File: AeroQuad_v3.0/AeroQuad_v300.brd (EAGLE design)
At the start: 87.3 x 54.6 mm, 68 parts, among them U1 MPU-6050-1

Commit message: Eagle files including CAM file for latest beta run of AeroQuad32 boards.
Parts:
- removed ACCEL: BMA180, SparkFun:1X08_LOCK
- removed GYRO: ITG3200, SparkFun:1X07_LOCK
- removed LED: ULN2003A, CaranchoEngineering:DIL16
- removed LED_GND, LED_PWR: (no value), SparkFun:1X07_LOCK
- moved LEVELSHIFTIN 72.4 mm to (64.8, 41.9)
- moved LEVELSHIFTOUT 72.4 mm to (64.8, 31.8)
- moved SJ3 11.4 mm to (73.7, 24.1)
- moved R2 9.25 mm to (68.6, 19.1)
- moved SJ2 8.03 mm to (76.2, 24.1)
- moved R1 5.68 mm to (68.6, 20.3)
- moved U1 5.24 mm to (63.5, 25.4)
- moved C2 2.54 mm to (59.7, 17.8)
- moved SJ1 1.80 mm to (74.9, 26.7)
- moved C1 1.27 mm to (59.7, 21.6)
- moved C3 1.27 mm to (59.7, 19.1)
- moved C4 1.27 mm to (59.7, 20.3)
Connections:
- removed net N$10: LED.10, LED_GND.7
- removed net N$11: LED.11, LED_GND.6
- removed net N$12: LED.12, LED_GND.5
- removed net N$13: LED.13, LED_GND.4
- removed net N$14: LED.14, LED_GND.3
- removed net N$17: LED.15, LED_GND.2
- removed net P$16: LED.16, LED_GND.1
- net 3.3V: no longer ACCEL.1, ACCEL.4, ACCEL.8, GYRO.6, GYRO.7
- net GND: no longer ACCEL.2, ACCEL.6, GYRO.3, GYRO.5, LED.8
- net LED1: no longer LED.7
- net LED2: no longer LED.6
- net LED3: no longer LED.5
- net LED4: no longer LED.4
- net LED5: no longer LED.3
- net LED6: no longer LED.2
- net LED7: no longer LED.1
- net SCL-L: no longer ACCEL.5, GYRO.1
- net SDA-L: no longer ACCEL.7, GYRO.2
- net VIN: no longer LED_PWR.1, LED_PWR.2, LED_PWR.3, LED_PWR.4, LED_PWR.5, LED_PWR.6, LED_PWR.7
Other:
- board text added: "MOTOR OUTPUT"
- board text added: "RECEIVER INPUT"
- board text removed: "12V LED"
- board text removed: "ACCELEROMETER"
- board text removed: "GYRO"
- board text removed: "PWM ESC"
- board text removed: "RECEIVER"

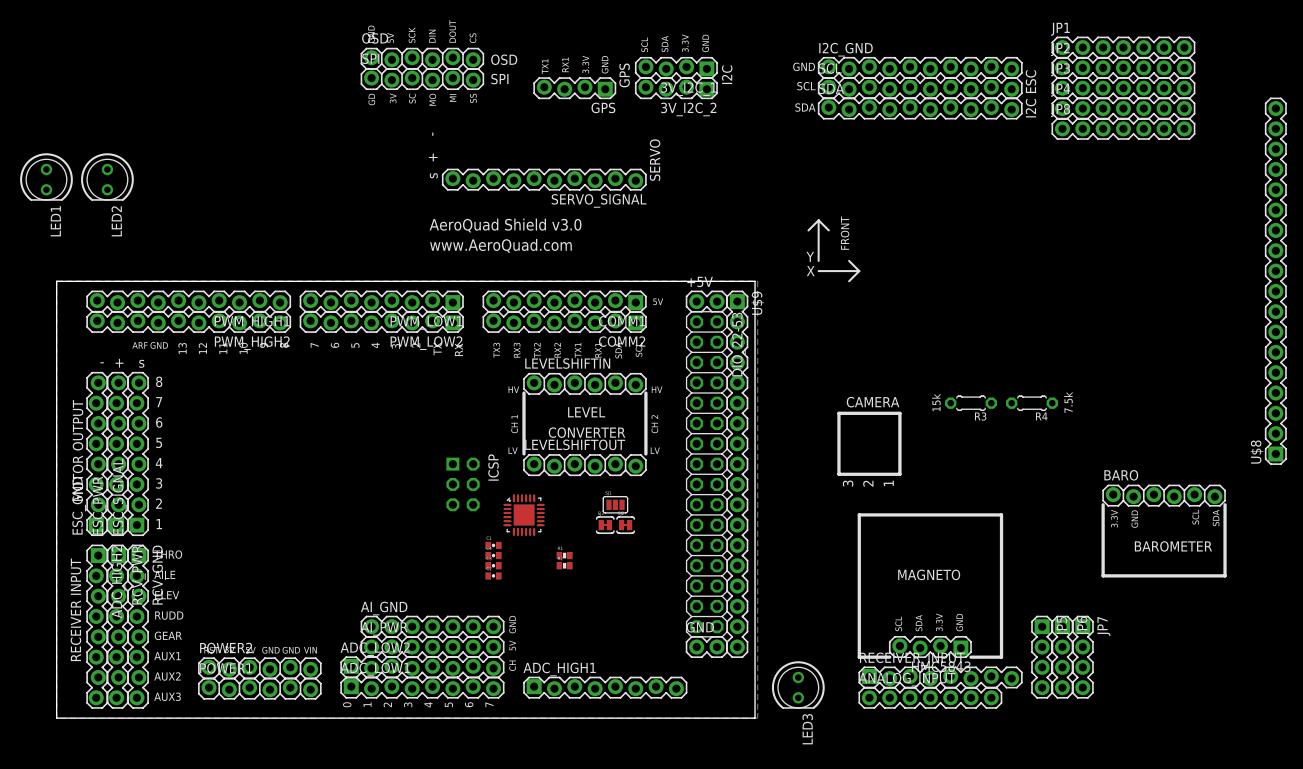
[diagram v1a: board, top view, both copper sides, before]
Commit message: reviewed MPU6000 circuit and connections to Due
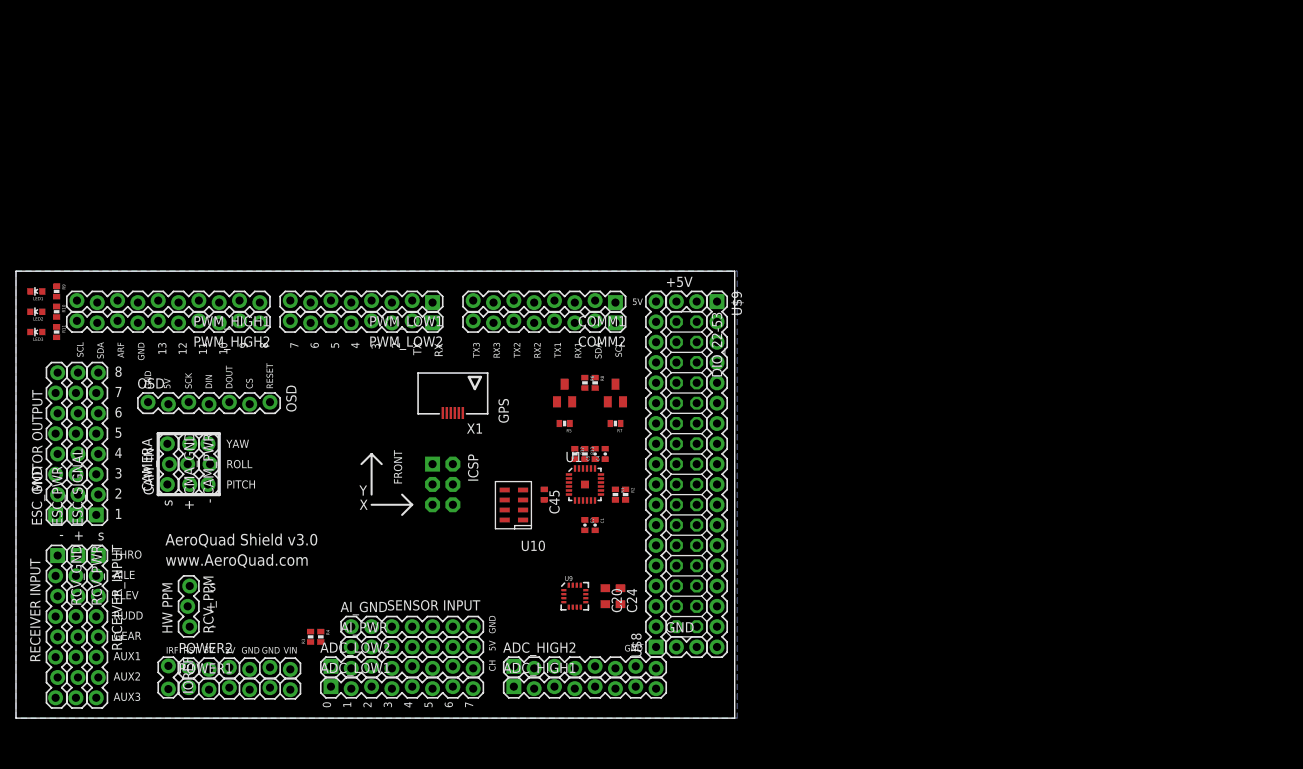
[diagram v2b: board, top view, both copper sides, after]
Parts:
- removed 3V_I2C_1, 3V_I2C_2, GPS, HMC5843: (no value), SparkFun:1X04_LOCK
- removed ANALOG_INPUT, JP1, JP2, JP3, JP4, JP8: (no value), SparkFun:1X07
- removed BARO: BMP085, SparkFun:1X06_LOCK
- removed C3: 0.1uF, SparkFun:0402-CAP
- removed I2C_GND, SCL, SDA, SERVO_SIGNAL: M10LOCK, SparkFun:1X10_LOCK
- removed JP5, JP6, JP7: (no value), SparkFun:1X04
- removed LEVELSHIFTIN, LEVELSHIFTOUT, SPI: (no value), SparkFun:1X06_LOCK
- removed SJ1: (no value), SparkFun:SJ_3_PASTE2&3
- removed SJ2, SJ3: (no value), SparkFun:SJ_2S-TRACE
- added C20, C24: 1uF (ESR), rcl:SMC_Z
- added C45: 0.1uF, rcl:C0402
- added C5: 2.2nF, SparkFun:0402-CAP
- added CAM_IN, CAM_PWR, CMA_GND, RCV_PPM: (no value), SparkFun:1X03_LOCK
- added IOREF: (no value), SparkFun:1X02_LOCK
- added R10, R11, R9: 1k, SparkFun:0402-RES
- added R12, R13, R5, R6, R7, R8: 10k, SparkFun:0402-RES
- added U$1, U$2: BSS138, ava:BSS138
- added U10: MS5611, DSP-TI:LGA08A
- added U9: HMC5883LSMD, SparkFun:16LPCC
- added X1: 06FLZ-SM1, con-jst:6FLZ-SM
- C1: value 0.1uF -> 10nF
- C2: value 2.2nF -> 0.1uF
- C4: value 10nF -> 0.1uF
- LED1: value (none) -> Green; device SparkFun:LED5MM -> SparkFun:LED-0603
- LED2: value (none) -> Yellow; device SparkFun:LED5MM -> SparkFun:LED-0603
- LED3: value (none) -> Red; device SparkFun:LED5MM -> SparkFun:LED-0603
- OSD: device SparkFun:1X06_LOCK -> SparkFun:1X07_LOCK
- R3, R4: device resistor:0204/5 -> SparkFun:0402-RES
- U1: value MPU-6050-1 -> MPU-6000; device Testing:QFN-24-4MM2 -> 3DRobotics_Master_Library:QFN-24
- moved LED3 105.1 mm to (2.54, 48.3), turned to 90 degrees
- moved RECEIVER_INPUT 97.7 mm to (10.2, 20.3), turned to 270 degrees
- moved R4 93.6 mm to (38.1, 10.2), turned to 270 degrees
- moved R3 87.6 mm to (36.8, 10.2), turned to 90 degrees
- moved U$8 81.1 mm to (80.0, 8.89)
- moved ADC_HIGH2 53.9 mm to (62.2, 6.35), turned to 0 degrees
- moved OSD 51.4 mm to (16.5, 39.4)
- moved C4 18.9 mm to (73.7, 33.0), turned to 90 degrees
- moved LED2 18.8 mm to (2.54, 50.8), turned to 90 degrees
- moved LED1 14.0 mm to (2.54, 53.3), turned to 90 degrees
- moved C2 13.1 mm to (71.1, 24.1), turned to 270 degrees
- moved C1 13.0 mm to (72.4, 24.1), turned to 270 degrees
- moved R2 11.7 mm to (76.2, 27.9), turned to 270 degrees
- moved RCV_GND 10.2 mm to (5.08, 20.3)
- moved R1 9.92 mm to (74.9, 27.9), turned to 270 degrees
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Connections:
- removed net AD0: SJ1.2, U1.9
- removed net AUX_SCL: U1.7
- removed net AUX_SDA: U1.6
- removed net CLKIN: SJ2.2, U1.1
- removed net FSYNC: SJ3.2, U1.11
- removed net INT: U1.12
- removed net LED6: DIO_22-53.27, U$8.4
- removed net N$15: DIO_22-53.3, U$8.16
- removed net N$20: DIO_22-53.5, U$8.15
- removed net N$22: DIO_22-53.4, U$9.3
- removed net N$28: PWM_HIGH1.4, PWM_HIGH2.4
- removed net N$29: PWM_HIGH1.5, PWM_HIGH2.5
- removed net N$30: PWM_HIGH1.9, PWM_HIGH2.9
- removed net N$31: PWM_HIGH1.10, PWM_HIGH2.10
- removed net N$32: C2.1, U1.20
- removed net VCC: C3.1, R1.2, R2.2, SJ1.1, U1.13
- removed net VIO: C4.1, U1.8
- new net 3V3DIG: C45.1, U10.1, U10.2, U10.4, U10.5
- new net CAM_PITCH: CAM_IN.1, PWM_HIGH1.4, PWM_HIGH2.4
- new net CAM_ROLL: CAM_IN.2, PWM_HIGH1.5, PWM_HIGH2.5
- new net ESCPWR1: CAM_PWR.1, CAM_PWR.2, CAM_PWR.3, ESC_PWR.1
- new net ESCPWR2: ESC_PWR.2
- new net ESCPWR3: ESC_PWR.3
- new net ESCPWR4: ESC_PWR.4
- new net HWPPM: DIO_22-53.27, RCV_PPM.1, U$8.4
- new net MPU_CLK: DIO_22-53.5, U$8.15, U1.22
- new net MPU_CS: C1.1, DIO_22-53.3, R2.1, U$8.16, U1.8
- new net MPU_INT: DIO_22-53.4, U$9.3, U1.12
- new net N$10: LED1.A, R9.1
- new net N$11: LED2.A, R10.1
- new net N$12: LED3.A, R11.1
- new net N$40: C5.1, U1.20
- new net N$67: C20.+, C24.+, U9.10
- new net SCL1: PWM_HIGH1.10, PWM_HIGH2.10, U1.7
- new net SDA1: PWM_HIGH1.9, PWM_HIGH2.9, U1.6
- net 3.3V: now also C4.1, IOREF.1, IOREF.2, R1.2, R12.1, R13.1, R2.2, R5.2, R7.2, U$1.G, U$2.G, U1.13, X1.1; no longer 3V_I2C_1.2, 3V_I2C_2.2, BARO.1, GPS.2, HMC5843.2, LEVELSHIFTOUT.3, SPI.2
- net 5V: now also OSD.7, R6.2, R8.2, RCV_PPM.2; no longer LEVELSHIFTIN.3
- net GND: now also C20.-, C24.-, C45.2, C5.2, CMA_GND.1, CMA_GND.2, CMA_GND.3, LED1.C, LED2.C, LED3.C, RCV_PPM.3, U1.1, U1.11, U10.3, U9.11, U9.9, X1.2, X1.6; no longer 3V_I2C_1.1, 3V_I2C_2.1, BARO.2, C3.2, GPS.1, HMC5843.1, I2C_GND.1, I2C_GND.10, I2C_GND.2, I2C_GND.3, I2C_GND.4, I2C_GND.5, I2C_GND.6, I2C_GND.7, I2C_GND.8, I2C_GND.9, LED1.K, LED2.K, LED3.K, LEVELSHIFTIN.4, LEVELSHIFTOUT.4, SJ1.3, SJ2.1, SJ3.1, SPI.1
- net MISO: no longer SPI.5
- net MOSI: no longer SPI.4
- net N$18: no longer ANALOG_INPUT.6
- net N$19: no longer ANALOG_INPUT.7
- net N$33: now also C2.1; no longer C1.1
- net N$4: no longer ANALOG_INPUT.1
- net N$6: no longer ANALOG_INPUT.2
- net N$7: no longer ANALOG_INPUT.3
- net N$8: no longer ANALOG_INPUT.4
- net N$9: no longer ANALOG_INPUT.5
- net RDY2_LED: now also R10.2; no longer LED2.A
- net RDY3_LED: now also R11.2; no longer LED3.A
- net RDY_LED: now also CAM_IN.3, R9.2; no longer LED1.A
- net RX1: now also X1.3; no longer GPS.3
- net RX3: now also R1.1, U1.9
- net SCL: now also R13.2, R8.1, U$2.D; no longer LEVELSHIFTIN.6, R1.1, SCL.1, SCL.10, SCL.2, SCL.3, SCL.4, SCL.5, SCL.6, SCL.7, SCL.8, SCL.9
- net SCL-L: now also R7.1, U$2.S, U10.8; no longer 3V_I2C_1.4, 3V_I2C_2.4, BARO.5, HMC5843.4, LEVELSHIFTOUT.6
- net SCLK: no longer SPI.3
- net SDA: now also R12.2, R6.1, U$1.D; no longer LEVELSHIFTIN.1, R2.1, SDA.1, SDA.10, SDA.2, SDA.3, SDA.4, SDA.5, SDA.6, SDA.7, SDA.8, SDA.9
- net SDA-L: now also R5.1, U$1.S, U10.7; no longer 3V_I2C_1.3, 3V_I2C_2.3, BARO.6, HMC5843.3, LEVELSHIFTOUT.1
- net SERVO1: no longer SERVO_SIGNAL.1
- net SERVO10: no longer SERVO_SIGNAL.10
- net SERVO2: no longer SERVO_SIGNAL.2
- net SERVO3: no longer SERVO_SIGNAL.3
- net SERVO4: no longer SERVO_SIGNAL.4
- net SERVO5: no longer SERVO_SIGNAL.5
- net SERVO6: no longer SERVO_SIGNAL.6
- net SERVO7: no longer SERVO_SIGNAL.7
- net SERVO8: no longer SERVO_SIGNAL.8
- net SERVO9: no longer SERVO_SIGNAL.9
- net SS: no longer SPI.6
- net TX1: now also X1.4; no longer GPS.4
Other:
- board size 87.3 x 54.6 mm -> 89.8 x 55.9 mm
- board text added: "HW PPM"
- board text added: "IRF"
- board text added: "PITCH"
- board text added: "RESET"
- board text added: "ROLL"
- board text added: "SENSOR INPUT"
- board text added: "YAW"
- board text removed: "15k"
- board text removed: "3.3V"
- board text removed: "7.5k"
- board text removed: "BAROMETER"
- board text removed: "CH 1"
- board text removed: "CH 2"
- board text removed: "CONVERTER"
- board text removed: "GD"
- board text removed: "HV"
- board text removed: "I2C"
- board text removed: "I2C ESC"
- board text removed: "LEVEL"
- board text removed: "LV"
- board text removed: "MAGNETO"
- board text removed: "MI"
- board text removed: "MO"
- board text removed: "SC"
- board text removed: "SERVO"
- board text removed: "SPI"
- board text removed: "SS"

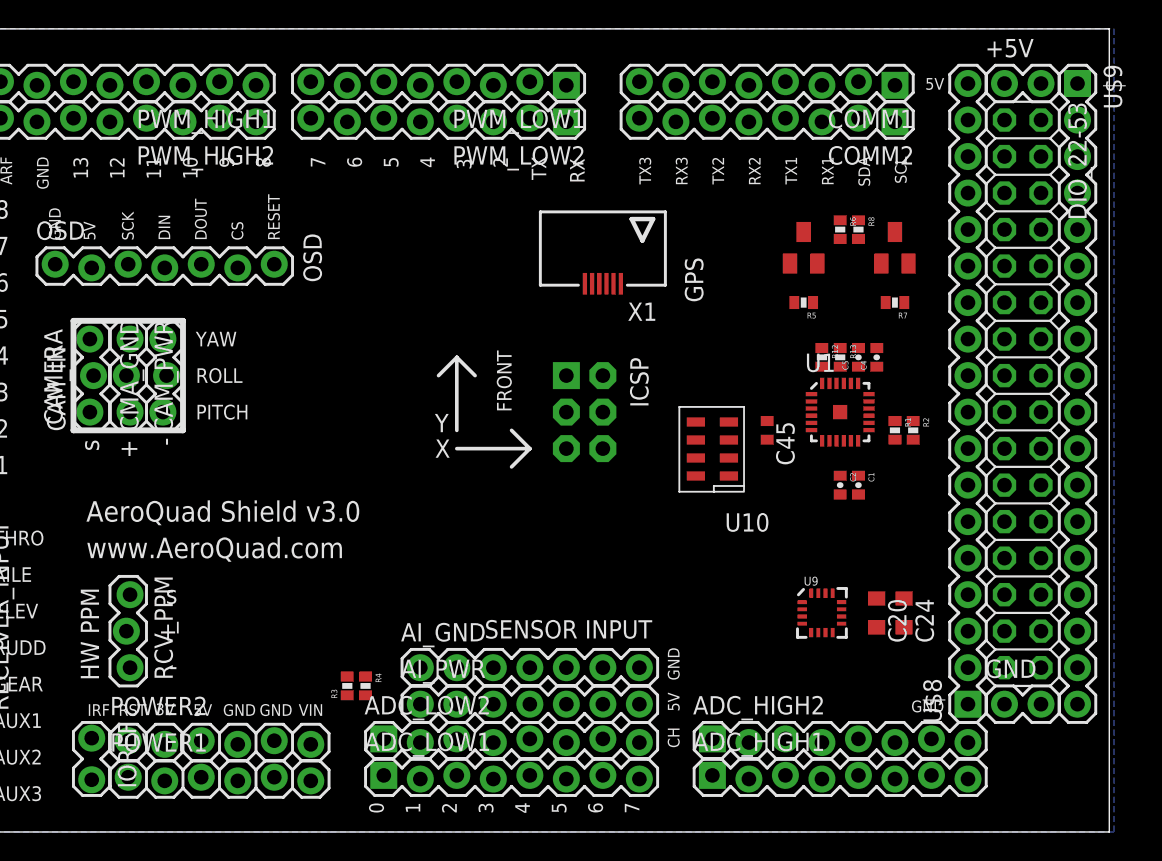
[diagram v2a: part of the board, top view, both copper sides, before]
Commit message: updated v2.1.3 shield with fixed 3.3V for GPS and added 5V reset line for OSD
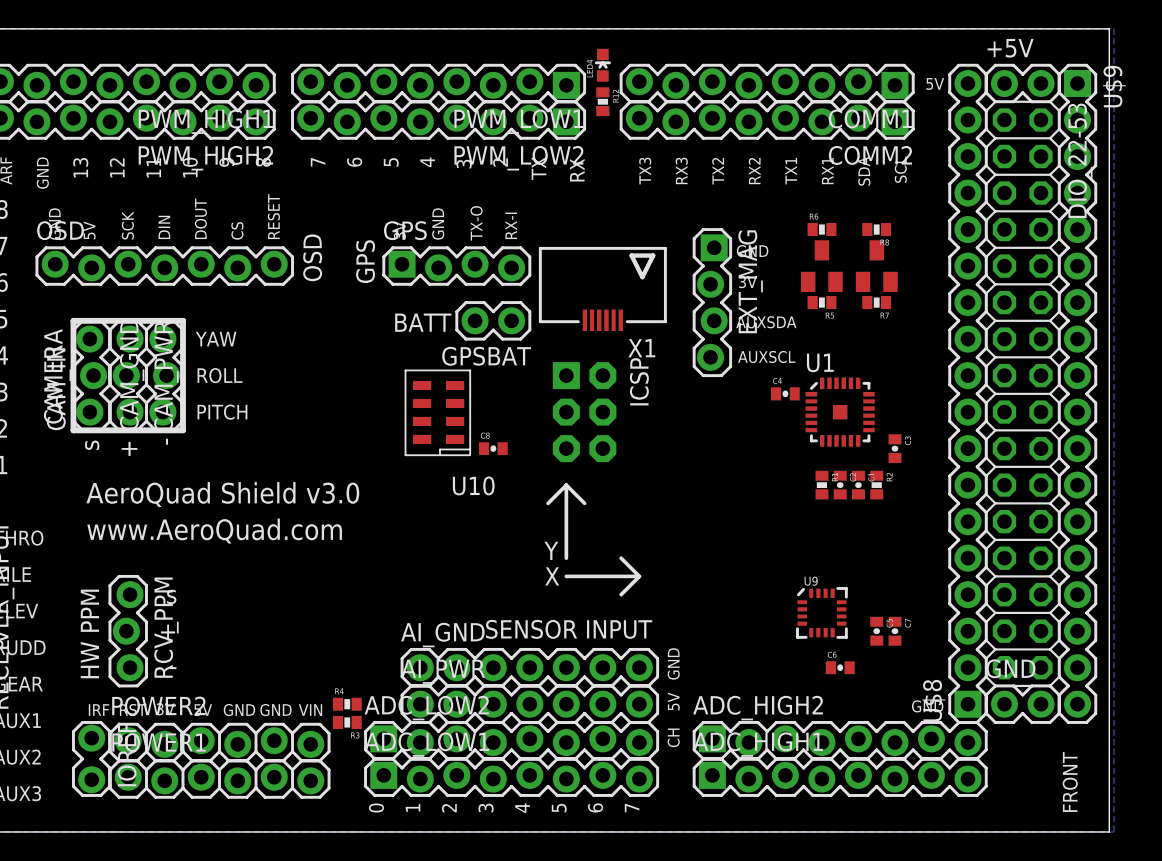
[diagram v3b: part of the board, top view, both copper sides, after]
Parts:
- removed C20, C24: 1uF (ESR), rcl:SMC_Z
- removed C45: 0.1uF, rcl:C0402
- removed R13: 10k, SparkFun:0402-RES
- added C3, C7: 0.1uF, SparkFun:0402-CAP
- added C6: 0.22uF, SparkFun:0402-CAP
- added C8: 100nF, SparkFun:0402-CAP
- added EXT_MAG, GPS: (no value), SparkFun:1X04_LOCK
- added GPSBAT: (no value), SparkFun:1X02
- added LED4: Green, SparkFun:LED-0603
- C4: value 0.1uF -> 2.2nF
- C5: value 2.2nF -> 4.7uF
- R12: value 10k -> 1k
- moved R12 23.4 mm to (54.6, 50.8)
- moved U10 19.2 mm to (43.2, 29.2)
- moved C5 19.1 mm to (73.7, 14.0), turned to 270 degrees
- moved C4 6.84 mm to (67.3, 30.5), turned to 0 degrees
- moved R1 6.35 mm to (69.8, 24.1)
- moved R2 4.58 mm to (73.7, 24.1)
- moved R3 2.54 mm to (36.8, 7.62), turned to 180 degrees
- moved X1 2.54 mm to (54.6, 38.1)
- moved U$2 1.80 mm to (73.7, 39.4)
- moved R4 1.80 mm to (36.8, 8.89), turned to 0 degrees
- moved U$1 1.80 mm to (69.8, 39.4)
- moved R6 1.27 mm to (69.8, 41.9), turned to 0 degrees
- moved R7 1.27 mm to (73.7, 36.8)
- moved R5 1.27 mm to (69.8, 36.8)
- moved R8 1.27 mm to (73.7, 41.9), turned to 180 degrees
- renumbered CMA_GND to CAM_GND
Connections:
- net N$18 renamed AI6
- net N$19 renamed AI7
- net N$4 renamed AI1
- net N$6 renamed AI2
- net N$7 renamed AI3
- net N$8 renamed AI4
- net N$9 renamed AI5
- removed net 3V3DIG: C45.1, U10.1, U10.2, U10.4, U10.5
- removed net N$67: C20.+, C24.+, U9.10
- new net GLED: R12.2, X1.6
- new net N$13: C5.1, U9.10
- new net N$14: EXT_MAG.4, U1.7
- new net N$15: EXT_MAG.3, U1.6
- new net N$17: IOREF.1, IOREF.2
- new net N$20: C6.1, U9.8
- new net N$22: C6.2, U9.12
- new net N$4: LED4.A, R12.1
- new net N$8: GPSBAT.2, X1.5
- net 3.3V: now also C3.1, C7.1, C8.1, EXT_MAG.2, GPS.1, U10.1, U10.2, U10.4, U10.5, U9.13, U9.2, U9.4, X1.4; no longer C4.1, IOREF.1, IOREF.2, R12.1, R13.1, X1.1
- net GND: now also C3.2, C7.2, C8.2, EXT_MAG.1, GPS.2, GPSBAT.1, LED4.C, X1.3; no longer C20.-, C24.-, C45.2, X1.2, X1.6
- net N$40: now also C4.1; no longer C5.1
- net RX1: now also GPS.3, X1.2; no longer X1.3
- net SCL: no longer R13.2, U1.23
- net SCL-L: now also U1.23, U9.1
- net SCL1: no longer U1.7
- net SDA: no longer R12.2, U1.24
- net SDA-L: now also U1.24, U9.16
- net SDA1: no longer U1.6
- net TX1: now also GPS.4, X1.1; no longer X1.4
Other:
- board text added: "AUXSCL"
- board text added: "AUXSDA"
- board text added: "BATT"
- board text added: "RX-I"
- board text added: "TX-O"
